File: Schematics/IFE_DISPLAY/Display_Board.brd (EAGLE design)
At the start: 160 x 100 mm, 77 parts, among them IC1 EP2C5T144, Q1 16MHz, U1 EPCS1SI8N, U2 MX150_8_PIN, U4 HEX_CONVERTER, U5 HEX_CONVERTER, U6 TPS5420D, U7 MCP1826S-1802E/DB, U8 TPS5420D, X3 16MHz

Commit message: Finalizing Display Schematic
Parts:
- removed AS, JTAG: (no value), pinhead:2X05
- removed C1, C16: 4.7uF, resistor:C0805K
- removed C10, C12, C18, C19: 47uF, rcl:C0805K
- removed C11: 0.1u, rcl:C0805K
- removed C13, C20: 1800pF, rcl:C0805K
- removed C14, C21: 0.1uF, rcl:C0805K
- removed C15, C22: 150pF, rcl:C0805K
- removed C17, C2: 0.01uF, resistor:C0805K
- removed C23, C5: 220u, Capacitors:C1206
- removed D2, D3: (no value), adafruit:SMADIODE
- removed FUSE1, FUSE2: MINI297-3568, Fuse:3568
- removed IC1: EP2C5T144, altera-cyclone-II:TQFP144
- removed L1: 23uH, Inductors:MSS7348
- removed L2, L4: 20uH, Inductors:MSS7348
- removed L3: 58uH, Inductors:MSS7348
- removed QG1: SM77H, crystal:SM77H
- removed R1, R15, R2: 1K, resistor:R0805
- removed R11, R16, R17, R20, R21, R22: 10k, rcl:R0805
- removed R14: 10K, resistor:R0805
- removed R18, R23: 5.9k, rcl:R0805
- removed R19, R24: 549, rcl:R0805
- removed U6, U8: TPS5420D, Texas Instruments_By_element14_Batch_1:SOIC127P600X175-8N
- removed U7: MCP1826S-1802E/DB, Microchip_By_element14_Batch_1:SOT230P700X180-4N
- added AS1, JTAG1: (no value), pinhead:2X05
- added C24, C40: 220u, Capacitors:C1206
- added C25: 0.1u, rcl:C0805K
- added C26, C33: 4.7uF, resistor:C0805K
- added C27, C34: 0.01uF, resistor:C0805K
- added C28, C29, C35, C36: 47uF, rcl:C0805K
- added C30, C37: 1800pF, rcl:C0805K
- added C31, C38: 0.1uF, rcl:C0805K
- added C32, C39: 150pF, rcl:C0805K
- added D4, D5: (no value), adafruit:SMADIODE
- added FUSE3, FUSE4: MINI297-3568, Fuse:3568
- added IC2: EP2C5T144, altera-cyclone-II:TQFP144
- added L5, L8: 20uH, Inductors:MSS7348
- added L6: 23uH, Inductors:MSS7348
- added L7: 58uH, Inductors:MSS7348
- added Q2: MMBT3904L, transistor-npn:SOT23-BEC
- added QG2: SM77H, crystal:SM77H
- added R25: 76, resistor:R0805
- added R26: 5.2k, resistor:R0805
- added R27, R28, R33: 1K, resistor:R0805
- added R29, R30, R31, R32: 10K, resistor:R0805
- added R34: 10k, rcl:R0805
- added R35: 5.9k, rcl:R0805
- added R36: 549, rcl:R0805
- added U$1: 776280-1, IFE_AMPSEAL_Conn:776280-1
- added U10, U9: TPS5420D, Texas Instruments_By_element14_Batch_1:SOIC127P600X175-8N
- R12: value 10K -> 5.9k; device resistor:R0805 -> rcl:R0805
- R13: value 10K -> 549; device resistor:R0805 -> rcl:R0805
- R3: value 10K -> 10k; device resistor:R0805 -> rcl:R0805
- U1: value EPCS1SI8N -> MCP1826S-1802E/DB; device Altera_By_element14_Batch_1:SOIC127P600X175-8N -> Microchip_By_element14_Batch_1:SOT230P700X180-4N
- U2: value MX150_8_PIN -> EPCS1SI8N; device Connectors:MX150_8 -> Altera_By_element14_Batch_1:SOIC127P600X175-8N
- moved R3 517.0 mm to (-90.2, -436.9)
- moved R13 498.0 mm to (-64.8, -430.5)
- moved R12 497.9 mm to (-77.5, -430.5)
- moved U1 440.9 mm to (-50.8, -392.4)
- moved U2 369.6 mm to (-61.0, -334.0)
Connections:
- removed net N$10: C2.2, D2.C, L1.P$1, U6.8
- removed net N$11: FUSE2.P$1, FUSE2.P$4, L4.P$1
- removed net N$12: R11.1, R16.2, U6.5
- removed net N$14: C14.2, R19.2
- removed net N$15: C13.2, C14.1, C15.1, R17.1, R18.2, U6.4
- removed net N$16: C17.1, U8.1
- removed net N$17: C17.2, D3.C, L3.P$1, U8.8
- removed net N$18: R20.1, R21.2, U8.5
- removed net N$19: C20.2, C21.1, C22.1, R22.1, R23.2, U8.4
- removed net N$20: C21.2, R24.2
- removed net N$8: FUSE1.P$1, FUSE1.P$4, L2.P$1
- removed net N$9: C2.1, U6.1
- removed net TXD_3_3: U5.15
- new net N$13: Q2.B, R26.1
- new net N$21: IC2.82, R29.1
- new net N$22: C27.1, U9.1
- new net N$23: C27.2, D4.C, L6.P$1, U9.8
- new net N$25: C30.2, C31.1, C32.1, R12.2, R3.1, U9.4
- new net N$26: C31.2, R13.2
- new net N$27: C34.1, U10.1
- new net N$28: C34.2, D5.C, L7.P$1, U10.8
- new net N$30: C37.2, C38.1, C39.1, R34.1, R35.2, U10.4
- new net N$31: C38.2, R36.2
- new net N$32: FUSE4.P$1, FUSE4.P$4, L8.P$1
- net +12V: now also C24.1, C26.1, C33.1, L5.P$2, U10.5, U10.7, U9.5, U9.7; no longer C1.1, C16.1, C5.1, L2.P$2, R11.2, R20.2, U6.7, U8.7
- net +24V: now also C40.1, L8.P$2, R25.2; no longer C23.1, L4.P$2
- net +3V3: now also AS1.4, C28.1, C29.1, C30.1, IC2.102, IC2.116, IC2.127, IC2.138, IC2.23, IC2.29, IC2.46, IC2.5, IC2.54, IC2.66, IC2.77, IC2.95, JTAG1.4, L6.P$2, QG2.4, R28.1, R29.2, R31.2, R32.2, R33.2, U1.1, U2.3, U2.7, U2.8; no longer AS.4, C10.1, C12.1, C13.1, IC1.102, IC1.116, IC1.127, IC1.138, IC1.23, IC1.29, IC1.46, IC1.5, IC1.54, IC1.66, IC1.77, IC1.95, JTAG.4, L1.P$2, QG1.4, R13.2, R14.2, R15.2, R17.2, R2.1, R7.2, U1.3, U1.7, U1.8, U3.18, U3.4, U3.6, U7.1
- net +5V: now also C35.1, C36.1, C37.1, L7.P$2, R34.2, R7.2, U3.18, U3.4, U3.6; no longer C18.1, C19.1, C20.1, L3.P$2, R22.2
- net 50_MHZ: now also IC2.17, QG2.3; no longer IC1.17, QG1.3
- net ASDO: now also AS1.9, IC2.1, U2.5; no longer AS.9, IC1.1, U1.5
- net BLUE_0: now also IC2.52; no longer IC1.52
- net BLUE_1: now also IC2.53; no longer IC1.53
- net BLUE_2: now also IC2.55; no longer IC1.55
- net BLUE_3: now also IC2.57; no longer IC1.57
- net BLUE_4: now also IC2.58; no longer IC1.58
- net BLUE_5: now also IC2.59; no longer IC1.59
- net BLUE_6: now also IC2.60; no longer IC1.60
- net BLUE_7: now also IC2.63; no longer IC1.63
- net CANH: now also U$1.3; no longer U2.8
- net CANL: now also U$1.5; no longer U2.1
- net CONF_DONE: now also AS1.3, IC2.83, R32.1; no longer AS.3, IC1.83, R14.1
- net DATA0: now also AS1.7, IC2.14, U2.2; no longer AS.7, IC1.14, U1.2
- net DCLK: now also AS1.1, IC2.15, U2.6; no longer AS.1, IC1.15, U1.6
- net DISP_CLK: now also IC2.3
- net DISP_DEN: now also IC2.9
- net DISP_EN: now also IC2.4
- net DISP_HSYNC: now also IC2.7
- net DISP_LEDA: now also R25.1
- net DISP_LEDK: now also Q2.C
- net DISP_PWM: now also R26.2
- net DISP_VSYNC: now also IC2.8
- net FPGA_D0_3_3: now also IC2.142; no longer IC1.142
- net FPGA_D1_3_3: now also IC2.141; no longer IC1.141
- net FPGA_D2_3_3: now also IC2.139; no longer IC1.139
- net FPGA_D3_3_3: now also IC2.137; no longer IC1.137
- net FPGA_R0_3_3: now also IC2.136; no longer IC1.136
- net FPGA_R1_3_3: now also IC2.135; no longer IC1.135
- net FPGA_R2_3_3: now also IC2.134; no longer IC1.134
- net FPGA_R3_3_3: now also IC2.133; no longer IC1.133
- net FPGA_RSEL_3_3: now also IC2.144; no longer IC1.144
- net FPGA_W_3_3: now also IC2.143; no longer IC1.143
- net GND: now also AS1.10, AS1.2, C24.2, C25.2, C26.2, C28.2, C29.2, C32.2, C33.2, C35.2, C36.2, C39.2, C40.2, D4.A, D5.A, IC2.105, IC2.106, IC2.108, IC2.110, IC2.111, IC2.117, IC2.123, IC2.128, IC2.130, IC2.140, IC2.19, IC2.33, IC2.34, IC2.36, IC2.38, IC2.39, IC2.49, IC2.56, IC2.6, IC2.61, IC2.68, IC2.78, IC2.84, IC2.85, IC2.98, JTAG1.10, JTAG1.2, Q2.E, QG2.2, R12.1, R13.1, R27.1, R30.2, R35.1, R36.1, U$1.1, U1.2, U10.6, U2.4, U9.6; no longer AS.10, AS.2, C1.2, C10.2, C11.2, C12.2, C15.2, C16.2, C18.2, C19.2, C22.2, C23.2, C5.2, D2.A, D3.A, IC1.105, IC1.106, IC1.108, IC1.110, IC1.111, IC1.117, IC1.123, IC1.128, IC1.130, IC1.140, IC1.19, IC1.33, IC1.34, IC1.36, IC1.38, IC1.39, IC1.49, IC1.56, IC1.6, IC1.61, IC1.68, IC1.78, IC1.84, IC1.85, IC1.98, JTAG.10, JTAG.2, QG1.2, R1.1, R12.2, R16.1, R18.1, R19.1, R21.1, R23.1, R24.1, U2.7, U6.6, U7.2, U7.4, U8.6
- net GREEN_0: now also IC2.41; no longer IC1.41
- net GREEN_1: now also IC2.42; no longer IC1.42
- net GREEN_2: now also IC2.43; no longer IC1.43
- net GREEN_4: now also IC2.44; no longer IC1.44
- net GREEN_5: now also IC2.45; no longer IC1.45
- net GREEN_6: now also IC2.47; no longer IC1.47
- net GREEN_7: now also IC2.48; no longer IC1.48
- net GREEN_8: now also IC2.51; no longer IC1.51
- net LED1: now also IC2.129; no longer IC1.129
- net LED2: now also IC2.132; no longer IC1.132
- net N$1: now also FUSE3.P$1, FUSE3.P$4, L5.P$1; no longer IC1.82, R3.1
- net NCE: now also AS1.6, IC2.16, R30.1; no longer AS.6, IC1.16, R12.1
- net NCONFIG: now also AS1.5, IC2.20, R31.1; no longer AS.5, IC1.20, R13.1
- net NCSO: now also AS1.8, IC2.2, U2.1; no longer AS.8, IC1.2, U1.1
- net PWR_IN_12: now also FUSE3.P$2, FUSE3.P$3, U$1.4; no longer FUSE1.P$2, FUSE1.P$3, U2.2
- net PWR_IN_24: now also FUSE4.P$2, FUSE4.P$3, U$1.2; no longer FUSE2.P$2, FUSE2.P$3
- net RED_0: now also IC2.25; no longer IC1.25
- net RED_1: now also IC2.26; no longer IC1.26
- net RED_2: now also IC2.27; no longer IC1.27
- net RED_3: now also IC2.28; no longer IC1.28
- net RED_4: now also IC2.30; no longer IC1.30
- net RED_5: now also IC2.31; no longer IC1.31
- net RED_6: now also IC2.32; no longer IC1.32
- net RED_7: now also IC2.40; no longer IC1.40
- net TCK: now also IC2.12, JTAG1.1, R27.2; no longer IC1.12, JTAG.1, R1.2
- net TDI: now also IC2.13, JTAG1.9, R28.2; no longer IC1.13, JTAG.9, R2.2
- net TDO: now also IC2.10, JTAG1.3; no longer IC1.10, JTAG.3
- net TMS: now also IC2.11, JTAG1.5, R33.1; no longer IC1.11, JTAG.5, R15.1
- net TXD: no longer U5.14
- net VCC: now also C25.1, IC2.107, IC2.109, IC2.124, IC2.131, IC2.35, IC2.37, IC2.50, IC2.62, U1.3; no longer C11.1, IC1.107, IC1.109, IC1.124, IC1.131, IC1.35, IC1.37, IC1.50, IC1.62, U7.3

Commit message: Initial board organization. Time to route
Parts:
- removed X3: 16MHz, crystal:QS
- added Q3: 16MHz, adafruit:CTS406
- R35: value 5.9k -> 3.2k
- moved C35 530.8 mm to (65.4, 67.3), flipped to the bottom, turned to 90 degrees
- moved C36 530.3 mm to (68.6, 67.3), flipped to the bottom, turned to 90 degrees
- moved C24 529.7 mm to (76.2, 72.4), turned to 180 degrees
- moved C28 528.2 mm to (45.1, 67.3), flipped to the bottom, turned to 90 degrees
- moved C29 527.7 mm to (48.3, 67.3), flipped to the bottom, turned to 90 degrees
- moved C34 526.6 mm to (67.9, 72.4), turned to 270 degrees
- moved C27 523.2 mm to (47.6, 72.4), turned to 270 degrees
- moved D5 520.1 mm to (58.4, 66.0), turned to 180 degrees
- moved C40 519.3 mm to (76.2, 63.5), turned to 180 degrees
- moved D4 518.8 mm to (38.1, 66.0), turned to 180 degrees
- moved C33 518.7 mm to (59.1, 72.4), turned to 90 degrees
- moved C26 516.9 mm to (38.7, 72.4), turned to 90 degrees
- moved C37 516.2 mm to (57.8, 61.0), flipped to the bottom, turned to 90 degrees
- moved C39 516.0 mm to (55.2, 67.3), flipped to the bottom, turned to 90 degrees
- moved R35 515.2 mm to (61.6, 67.3), flipped to the bottom, turned to 270 degrees
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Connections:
- removed net GREEN_8: IC2.51
- net BLUE_0: now also IC2.40; no longer IC2.52
- net BLUE_1: now also IC2.32; no longer IC2.53
- net BLUE_2: now also IC2.31; no longer IC2.55
- net BLUE_3: now also IC2.30; no longer IC2.57
- net BLUE_4: now also IC2.28; no longer IC2.58
- net BLUE_5: now also IC2.27; no longer IC2.59
- net BLUE_6: now also IC2.26; no longer IC2.60
- net BLUE_7: now also IC2.25; no longer IC2.63
- net DISP_CLK: now also IC2.9; no longer IC2.3
- net DISP_DEN: now also IC2.3; no longer IC2.9
- net DISP_EN: now also IC2.8; no longer IC2.4
- net DISP_VSYNC: now also IC2.4; no longer IC2.8
- net GREEN_0: now also IC2.51; no longer IC2.41
- net GREEN_1: now also IC2.48; no longer IC2.42
- net GREEN_2: now also IC2.47; no longer IC2.43
- net GREEN_3: now also IC2.45
- net GREEN_5: now also IC2.43; no longer IC2.45
- net GREEN_6: now also IC2.42; no longer IC2.47
- net GREEN_7: now also IC2.41; no longer IC2.48
- net RED_0: now also IC2.63; no longer IC2.25
- net RED_1: now also IC2.60; no longer IC2.26
- net RED_2: now also IC2.59; no longer IC2.27
- net RED_3: now also IC2.58; no longer IC2.28
- net RED_4: now also IC2.57; no longer IC2.30
- net RED_5: now also IC2.55; no longer IC2.31
- net RED_6: now also IC2.53; no longer IC2.32
- net RED_7: now also IC2.52; no longer IC2.40
- net XTAL1: now also Q3.3; no longer X3.2
- net XTAL2: now also Q3.1; no longer X3.1
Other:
- board size 160 x 100 mm -> 118.1 x 83.8 mm

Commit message: Layout started
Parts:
- moved U$4 6.84 mm to (27.9, 12.7)
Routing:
- net RESET: track 0.00 -> 18.7 mm, vias 0 -> 1
- net CANL: track 0.00 -> 13.1 mm
- net GND: track 0.00 -> 12.3 mm
- net MISO: track 0.00 -> 11.6 mm
- net MOSI: track 0.00 -> 10.3 mm, vias 0 -> 1
- net SCK: track 0.00 -> 9.95 mm
- net +5V: track 0.00 -> 9.92 mm
- net CANH: track 0.00 -> 9.63 mm
- net TXCAN: track 0.00 -> 9.47 mm, vias 0 -> 1
- net XTAL2: track 0.00 -> 9.39 mm, vias 0 -> 1
- net 2515_OSC1: track 0.00 -> 9.25 mm, vias 0 -> 1
- net 2515_OSC2: track 0.00 -> 7.47 mm, vias 0 -> 1
- net RXCAN: track 0.00 -> 7.35 mm, vias 0 -> 1
- net XTAL1: track 0.00 -> 6.92 mm, vias 0 -> 1
- net N$5: track 0.00 -> 3.30 mm
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
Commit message: Routing and thinking about the FPC connector
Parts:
- moved L6 8.03 mm to (53.3, 64.8)
- moved R6 8.03 mm to (47.0, 63.5)
- moved C29 8.03 mm to (55.9, 69.8)
- moved C32 8.03 mm to (42.5, 69.8)
- moved R12 8.03 mm to (48.9, 69.8)
- moved C26 8.03 mm to (46.4, 74.9)
- moved C27 8.03 mm to (55.2, 74.9)
- moved R13 8.03 mm to (45.7, 76.2)
- moved R25 8.03 mm to (58.4, 19.1), turned to 180 degrees
- moved U9 8.03 mm to (50.8, 74.9)
- moved C30 8.03 mm to (45.1, 63.5)
- moved LED3 8.03 mm to (41.9, 63.5)
- moved R3 8.03 mm to (48.3, 63.5)
- moved C28 8.03 mm to (52.7, 69.8)
- moved C31 8.03 mm to (45.7, 69.8)
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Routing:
- net +3V3: track 0.00 -> 30.6 mm, vias 0 -> 1
- net N$25: track 0.00 -> 25.3 mm, vias 0 -> 1
- net N$30: track 0.00 -> 25.1 mm, vias 0 -> 1
- net NCSO: track 0.00 -> 20.8 mm, vias 0 -> 1
- net ASDO: track 0.00 -> 18.6 mm, vias 0 -> 1
- net +5V: track 9.92 -> 28.4 mm, vias 0 -> 1
- net +12V: track 0.00 -> 15.9 mm
- net N$23: track 0.00 -> 14.9 mm
- net DATA0: track 0.00 -> 14.3 mm, vias 0 -> 1
- net N$28: track 0.00 -> 14.2 mm
- net DCLK: track 0.00 -> 12.7 mm, vias 0 -> 1
- net TMS: track 0.00 -> 8.99 mm
- net LED2: track 0.00 -> 8.42 mm
- net LED1: track 0.00 -> 5.24 mm
- net N$31: track 0.00 -> 4.40 mm
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
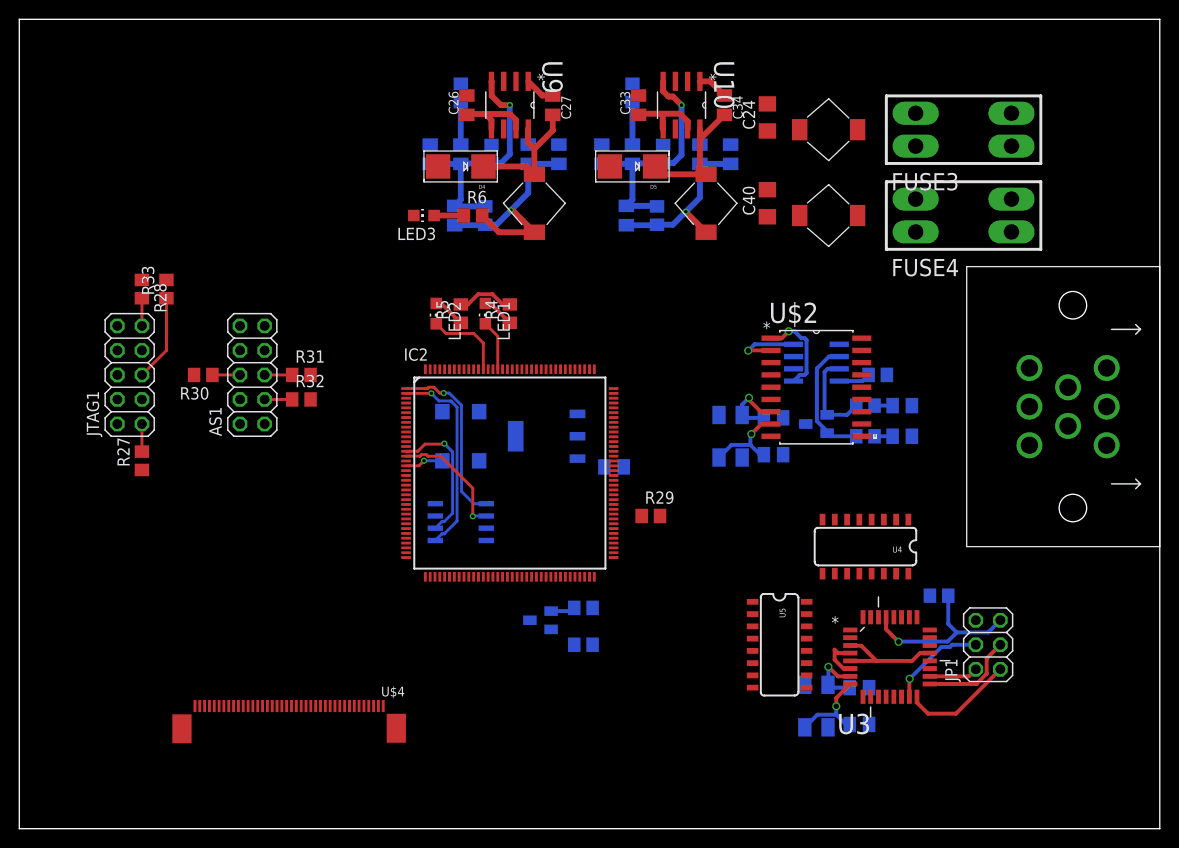
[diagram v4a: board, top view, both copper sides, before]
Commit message: More optimizations and working on interconnect for display board
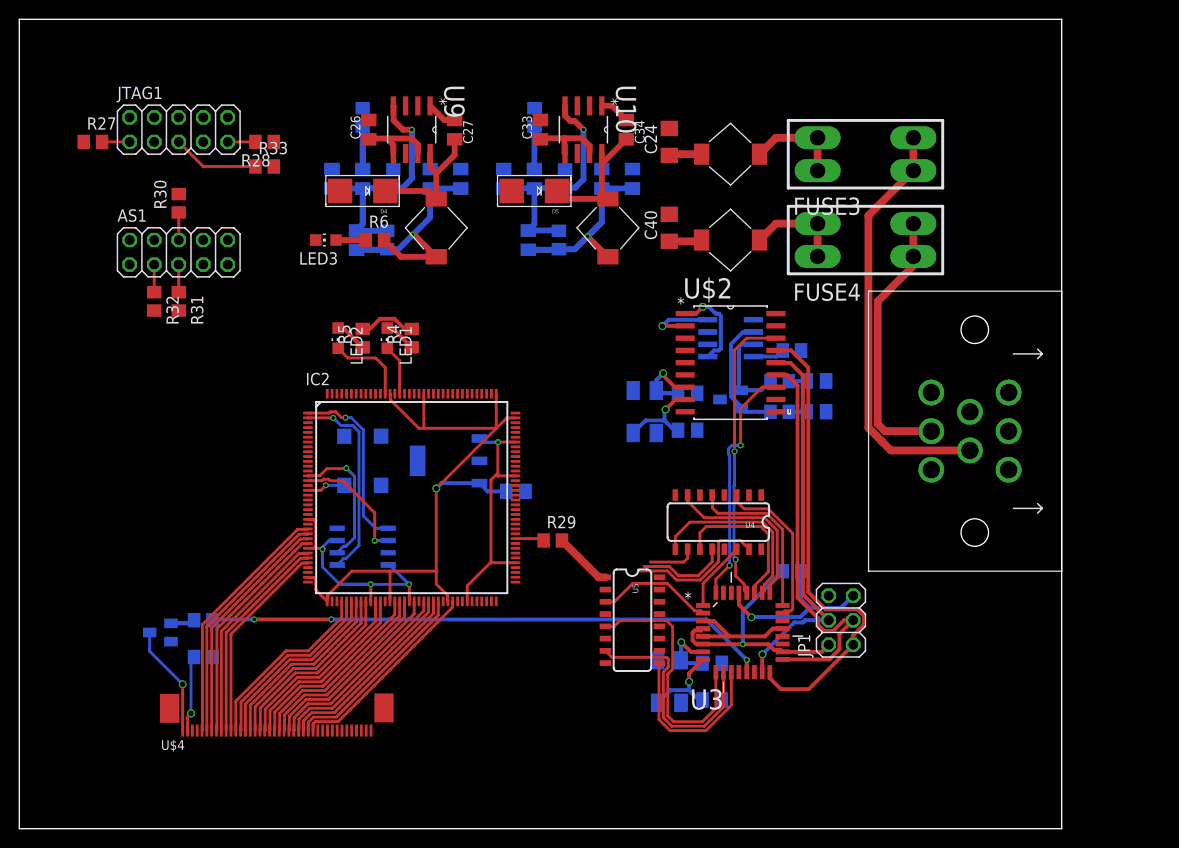
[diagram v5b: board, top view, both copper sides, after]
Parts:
- moved Q2 39.4 mm to (14.6, 20.3)
- moved R25 39.4 mm to (19.1, 17.8)
- moved R26 39.4 mm to (19.1, 21.6)
- moved R27 33.4 mm to (7.62, 71.1), turned to 0 degrees
- moved JTAG1 25.9 mm to (16.5, 72.4), turned to 0 degrees
- moved R28 19.8 mm to (25.4, 71.1), turned to 180 degrees
- moved R32 18.3 mm to (14.0, 54.6), turned to 270 degrees
- moved R30 18.0 mm to (16.5, 64.8), turned to 90 degrees
- moved R33 16.3 mm to (25.4, 68.6), turned to 0 degrees
- moved C3 15.5 mm to (71.8, 17.1)
- moved C4 15.5 mm to (71.8, 13.3)
- moved Q3 15.5 mm to (67.3, 15.2)
- moved R7 15.5 mm to (80.0, 26.7)
- moved JP1 15.5 mm to (85.1, 21.6)
- moved U3 15.5 mm to (74.9, 20.3)
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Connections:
- net BLUE_0: now also IC2.52; no longer IC2.40
- net BLUE_1: now also IC2.53; no longer IC2.32
- net BLUE_2: now also IC2.55; no longer IC2.31
- net BLUE_3: now also IC2.57; no longer IC2.30
- net BLUE_4: now also IC2.58; no longer IC2.28
- net BLUE_5: now also IC2.59; no longer IC2.27
- net BLUE_6: now also IC2.60; no longer IC2.26
- net BLUE_7: now also IC2.63; no longer IC2.25
- net DISP_CLK: now also IC2.3; no longer IC2.9
- net DISP_DEN: now also IC2.9; no longer IC2.3
- net DISP_EN: now also IC2.4; no longer IC2.8
- net DISP_VSYNC: now also IC2.8; no longer IC2.4
- net FPGA_D0_3_3: now also IC2.75; no longer IC2.142
- net FPGA_D1_3_3: now also IC2.76; no longer IC2.141
- net FPGA_D2_3_3: now also IC2.79; no longer IC2.139
- net FPGA_D3_3_3: now also IC2.80; no longer IC2.137
- net FPGA_R0_3_3: now also IC2.81; no longer IC2.136
- net FPGA_R1_3_3: now also IC2.86; no longer IC2.135
- net FPGA_R2_3_3: now also IC2.87; no longer IC2.134
- net FPGA_R3_3_3: now also IC2.92; no longer IC2.133
- net FPGA_RSEL_3_3: now also IC2.73; no longer IC2.144
- net FPGA_W_3_3: now also IC2.74; no longer IC2.143
- net GREEN_0: now also IC2.41; no longer IC2.51
- net GREEN_1: now also IC2.42; no longer IC2.48
- net GREEN_2: now also IC2.43; no longer IC2.47
- net GREEN_3: now also IC2.44; no longer IC2.45
- net GREEN_4: now also IC2.45; no longer IC2.44
- net GREEN_5: now also IC2.47; no longer IC2.43
- net GREEN_6: now also IC2.48; no longer IC2.42
- net GREEN_7: now also IC2.51; no longer IC2.41
- net RED_0: now also IC2.25; no longer IC2.63
- net RED_1: now also IC2.26; no longer IC2.60
- net RED_2: now also IC2.27; no longer IC2.59
- net RED_3: now also IC2.28; no longer IC2.58
- net RED_4: now also IC2.30; no longer IC2.57
- net RED_5: now also IC2.31; no longer IC2.55
- net RED_6: now also IC2.32; no longer IC2.53
- net RED_7: now also IC2.40; no longer IC2.52
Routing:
- net VCC: track 0.00 -> 71.0 mm, vias 0 -> 1
- net DISP_PWM: track 0.00 -> 58.4 mm, vias 0 -> 3
- net +3V3: track 30.6 -> 88.6 mm, vias 1 -> 5
- net PWR_IN_12: track 0.00 -> 43.5 mm
- net MISO: track 11.6 -> 49.2 mm
- net SCK: track 9.95 -> 42.7 mm
- net ~CS_CAN: track 0.00 -> 30.5 mm, vias 0 -> 2
- net MOSI: track 10.3 -> 40.0 mm
- net PWR_IN_24: track 0.00 -> 28.2 mm
- net FPGA_REG1: track 0.00 -> 26.5 mm
- net RED_0: track 0.00 -> 26.0 mm
- net ~INT_CAN: track 0.00 -> 25.3 mm, vias 0 -> 2
- net RED_1: track 0.00 -> 25.2 mm
- net RED_2: track 0.00 -> 24.4 mm
- net FPGA_REG2: track 0.00 -> 24.1 mm
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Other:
- board size 118.1 x 83.8 mm -> 108 x 83.8 mm

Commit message: Board Complete, DRC Complete, Just have to add Name and IFE Logo
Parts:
- moved R29 1.27 mm to (55.2, 31.1)
- moved R27 1.27 mm to (7.62, 72.4), turned to 270 degrees
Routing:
- net +3V3: track 88.6 -> 338.8 mm, vias 5 -> 16
- net +24V: track 3.59 -> 140.5 mm, vias 0 -> 1
- net +5V: track 44.7 -> 134.0 mm, vias 2 -> 3
- net GND: track 11.9 -> 73.5 mm, vias 0 -> 25
- net CONF_DONE: track 2.86 -> 57.5 mm, vias 0 -> 6
- net TCK: track 2.86 -> 49.4 mm, vias 0 -> 1
- net +12V: track 19.3 -> 65.7 mm
- net TDO: track 0.00 -> 43.6 mm, vias 0 -> 1
- net DISP_CLK: track 0.00 -> 43.5 mm, vias 0 -> 2
- net TMS: track 8.99 -> 51.6 mm, vias 0 -> 1
- net TDI: track 2.86 -> 45.4 mm, vias 0 -> 1
- net DISP_EN: track 0.00 -> 42.5 mm, vias 0 -> 2
- net DISP_HSYNC: track 0.00 -> 38.3 mm, vias 0 -> 2
- net NCE: track 2.86 -> 40.6 mm
- net DISP_VSYNC: track 0.00 -> 37.3 mm, vias 0 -> 2
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- added copper zone on layer 1, net GND
- added copper zone on layer 16, net GND
